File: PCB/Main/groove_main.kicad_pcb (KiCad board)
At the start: 2 copper layers, 214 x 99 mm, 118 parts, among them J1 Left_X, J10 Left_Y, J11 Right_X, J12 Right_Y, J13 SW, J14 SW, J15 V, J16 LED, J17 LED, J18 G, J19 V, J2 Left_Y, J20 LED, J21 LED, J22 G, J23 SW, J24 SW, J25 V, J26 V, J27 G, J28 G, J29 HAP, J3 Right_X, J30 V, J31 HAP, J32 V, J4 Right_Y, J5 Left_X, J6 Left_Y, J7 Right_X, J8 Right_Y, J9 Left_X, Q1 AO3400A, Q2 AO3400A, SW1 SWITCH_SPST, SW2 SWITCH_SPST, SW3 SWITCH_SPST, SW4 SWITCH_SPST, SW5 SWITCH_SPST, U1 PiPico, U2 CD4052B, U3 LM4040DBZ-3

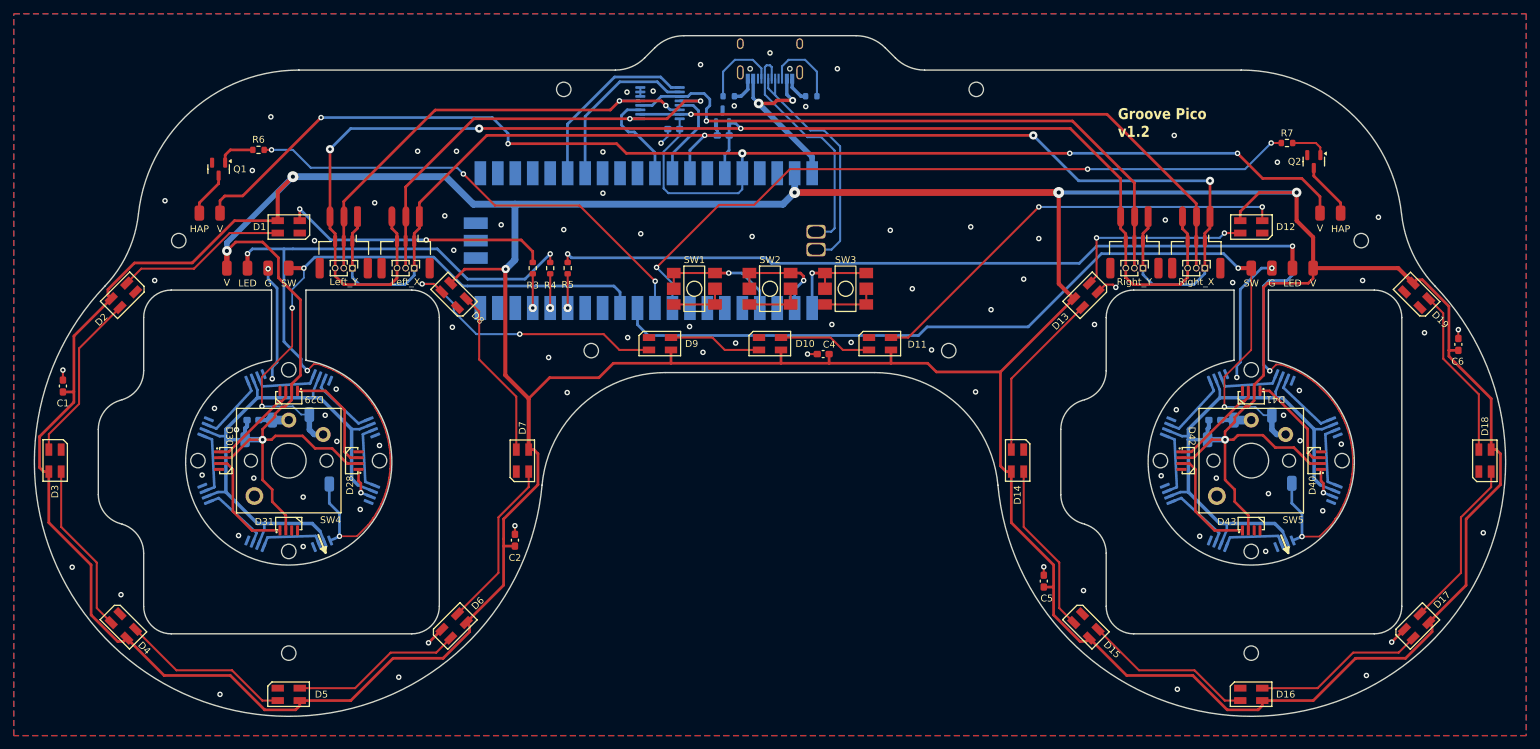
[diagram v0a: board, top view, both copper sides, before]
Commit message: PCB v1.21 (easier soldering)
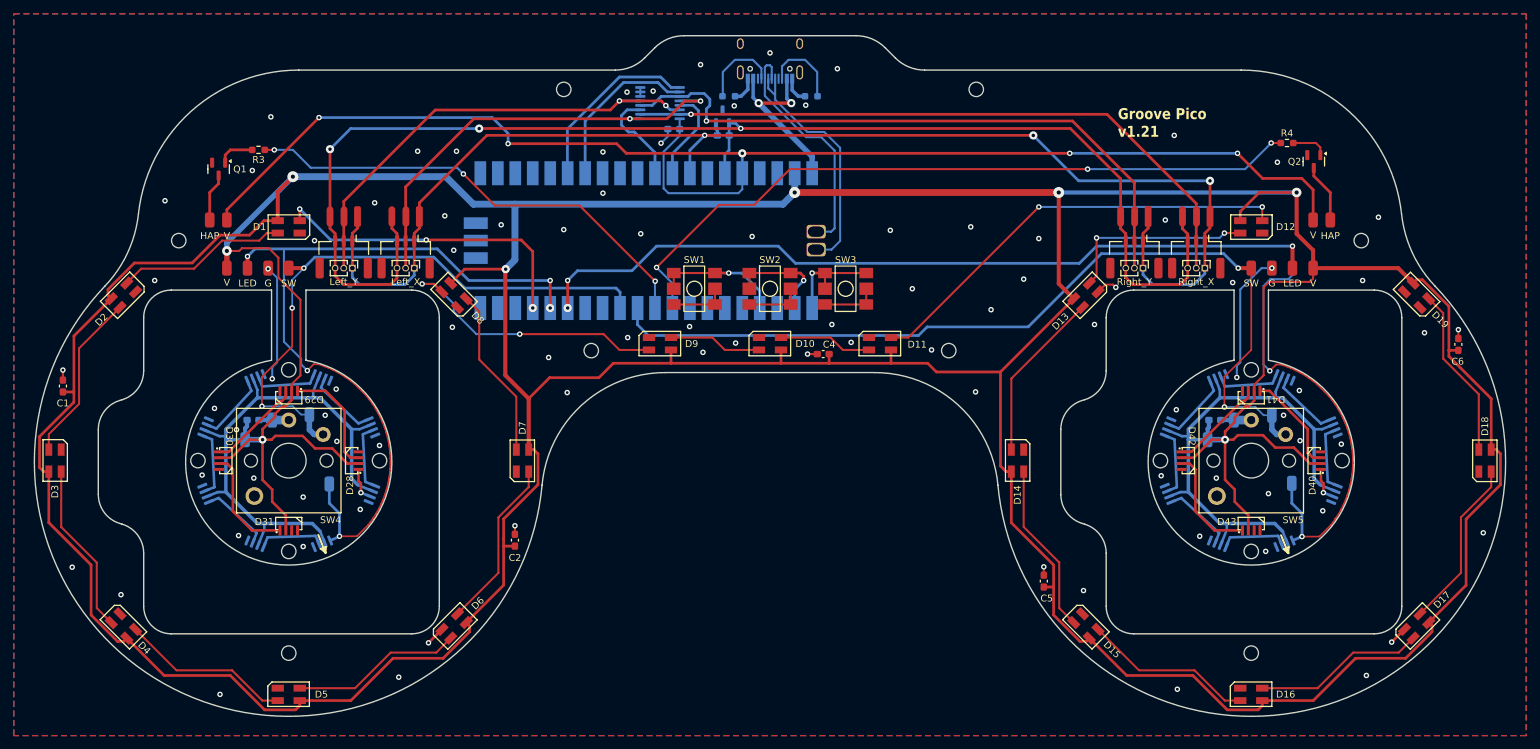
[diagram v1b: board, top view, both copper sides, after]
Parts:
- removed the R3 at (100.8, 85.4)
- removed the R4 at (103.3, 85.4)
- removed R5: 10, Resistor_SMD:R_0603_1608Metric
- R1, R2: footprint Resistor_SMD:R_0603_1608Metric -> Resistor_SMD:R_0603_1608Metric_Pad0.98x0.95mm_HandSolder
- R3: renamed from R6; footprint Resistor_SMD:R_0603_1608Metric -> Resistor_SMD:R_0603_1608Metric_Pad0.98x0.95mm_HandSolder
- R4: renamed from R7; footprint Resistor_SMD:R_0603_1608Metric -> Resistor_SMD:R_0603_1608Metric_Pad0.98x0.95mm_HandSolder
- moved J29 1.80 mm to (53.8, 78.4)
- moved J31 1.80 mm to (216.8, 78.4)
- moved J30 1.41 mm to (56.3, 78.4)
- moved J32 1.41 mm to (214.3, 78.4)
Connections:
- U1 pad 15: Net-(U1-GPIO11) -> Net-(D32-In)
- U1 pad 16: Net-(U1-GPIO12) -> Net-(D20-In)
- U1 pad 17: Net-(U1-GPIO13) -> Net-(D1-In)
- USB1 pad 13: unconnected-(USB1-SHIELD-Pad13) -> GND
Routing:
- net Net-(D1-In): track 39.7 -> 46.4 mm, vias 2 -> 3
- net Net-(D32-In): track 178.8 -> 184.1 mm, vias 4 -> 5
- net Net-(U1-GPIO13): track 4.98 -> 0.00 mm, vias 1 -> 0
- net Net-(U1-GPIO12): track 4.98 -> 0.00 mm, vias 1 -> 0
- net Net-(U1-GPIO11): track 4.98 -> 0.00 mm, vias 1 -> 0
- net Net-(D20-In): track 115.5 -> 116.6 mm, vias 4 -> 5
- net +5V: track 1049.3 -> 1048.6 mm
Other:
- board text added: "Groove Pico v1.21"
- board text removed: "Groove Pico v1.2"

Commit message: Improve voltage reference design
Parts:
- added R5: 100, Resistor_SMD:R_0603_1608Metric_Pad0.98x0.95mm_HandSolder, B.Cu at (132.3, 66.1)
- moved U3 0.10 mm to (128.4, 63.3)
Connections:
- net +3.3VADC renamed Vref
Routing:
- net +3V3: track 203.0 -> 209.6 mm
- net Net-(U1-GPIO26_ADC0): track 14.0 -> 15.4 mm
- net Vref: track 200.9 -> 202.1 mm
- net GND: track 96.5 -> 96.7 mm, vias 92 -> 94
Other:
- board text added: "Groove Pico v1.22"
- board text removed: "Groove Pico v1.21"
